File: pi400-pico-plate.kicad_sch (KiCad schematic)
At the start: 7 parts, among them J1 2.54mm socket RA, J2 2.54mm header, J3 2.54mm header, J4 2.54mm header, J5 2.54mm header, SW1 PTS815, U1 Pico

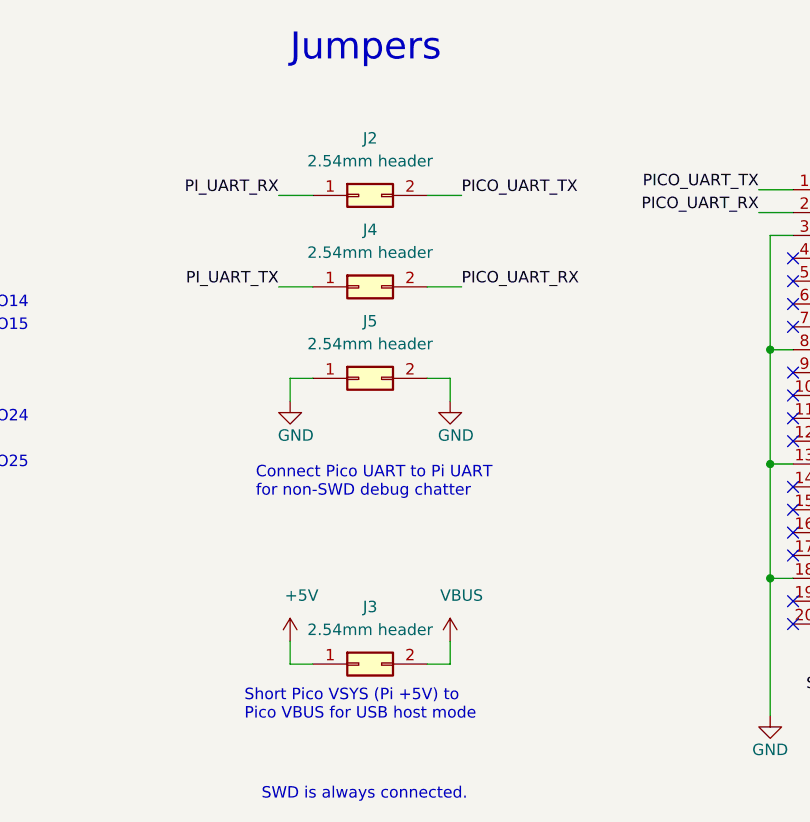
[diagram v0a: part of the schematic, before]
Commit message: Start rev B changes -- make UART jumpers cut-link, remove aux GND header
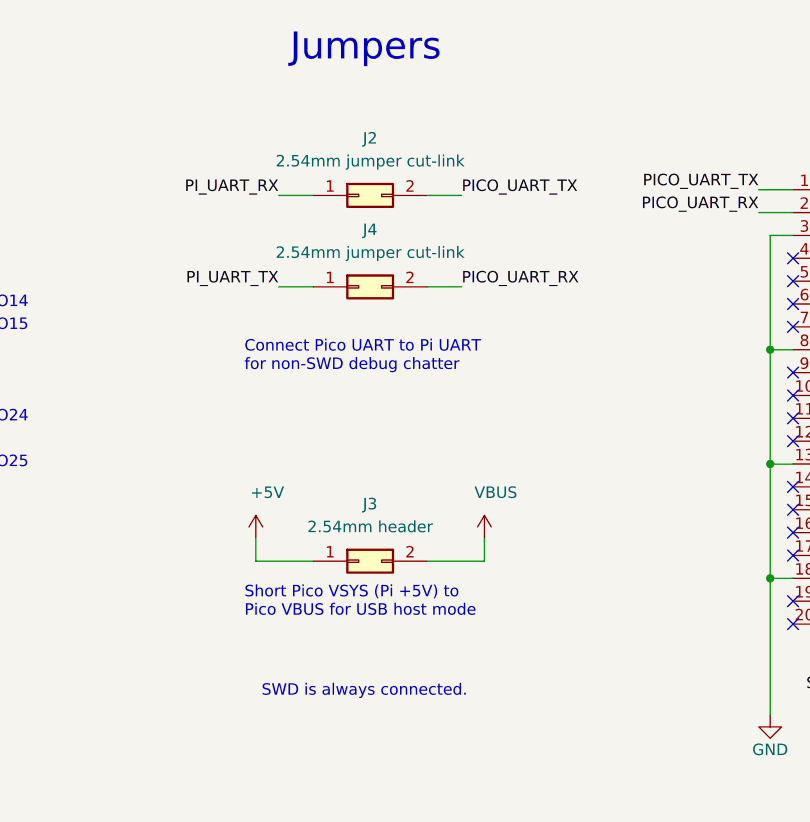
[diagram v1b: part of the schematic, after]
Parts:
- removed J5: 2.54mm header, Connector_PinHeader_2.54mm:PinHeader_2x01_P2.54mm_Vertical, symbol Connector_Generic:Conn_02x01
- J2, J4: value 2.54mm header -> 2.54mm jumper cut-link; footprint Connector_PinHeader_2.54mm:PinHeader_2x01_P2.54mm_Vertical -> pi400-pico-plate:2.54mm- jumper-closed
- J3: footprint Connector_PinHeader_2.54mm:PinHeader_2x01_P2.54mm_Vertical -> pi400-pico-plate:PinHeader_2x01_P2.54mm_Vertical
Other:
- moved on the sheet: J3

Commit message: Add indicator LEDs, trim bottom board edge by 0.5 mm (by Pico SWD pads)
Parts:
- added D1, D2, D3: LED, LED_SMD:LED_0805_2012Metric, symbol Device:LED
- added R1, R2, R3: 2k2, Resistor_SMD:R_0402_1005Metric, symbol Device:R
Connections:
- net GND: now also R3.2
- net PI_UART_RX: now also R2.2
- net PI_UART_TX: now also R1.2
- net SWCLK: now also D3.2 (A)
- net +3V3: now reaches J1.17 (Pin_17)
- net +3V3: now also D1.2 (A), D2.2 (A)
- new net: D2.1 (K), R2.1
- new net: D3.1 (K), R3.1
- new net: D1.1 (K), R1.1
- no-connect marks 53 -> 52
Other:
- note added: "Indicator LEDS"
- moved on the sheet: J1, J3

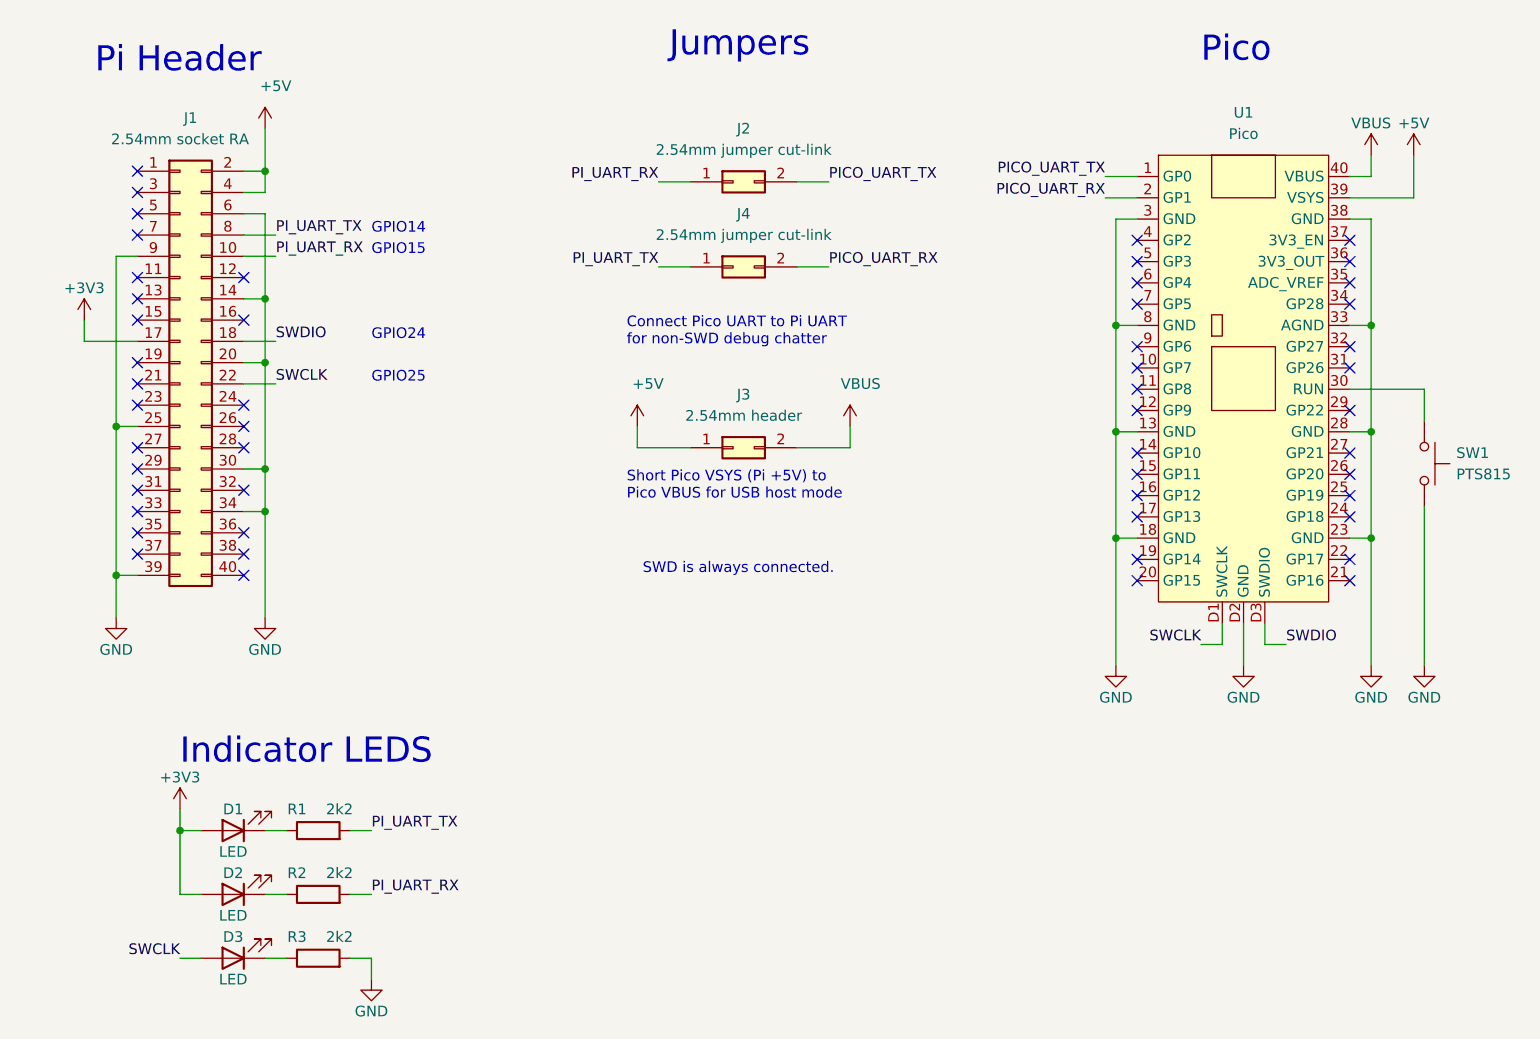
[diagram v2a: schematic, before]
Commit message: Add mounting holes for standoffs. Power layout changed as a result
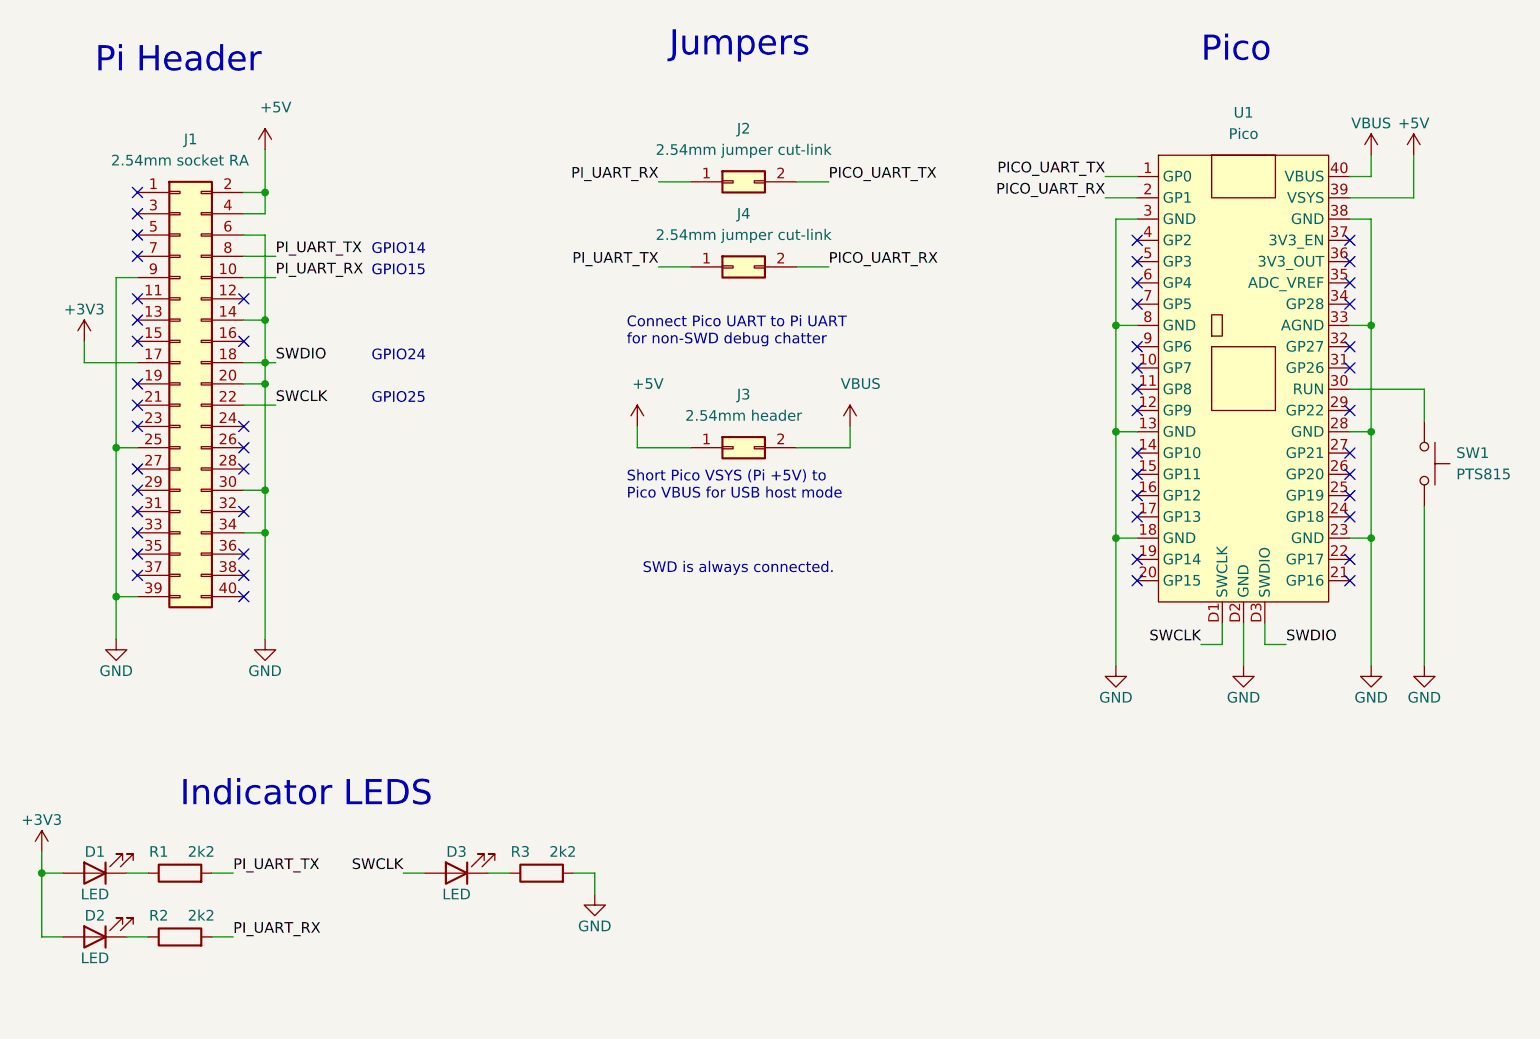
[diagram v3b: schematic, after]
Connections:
- net SWDIO is gone; now on net GND: J1.18 (Pin_18), U1.D3 (SWDIO)
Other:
- moved on the sheet: D1, D2, D3, J1, R1, R2, R3
